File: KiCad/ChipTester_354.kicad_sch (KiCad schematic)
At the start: 3 parts, among them SW1 7101MD9AQE

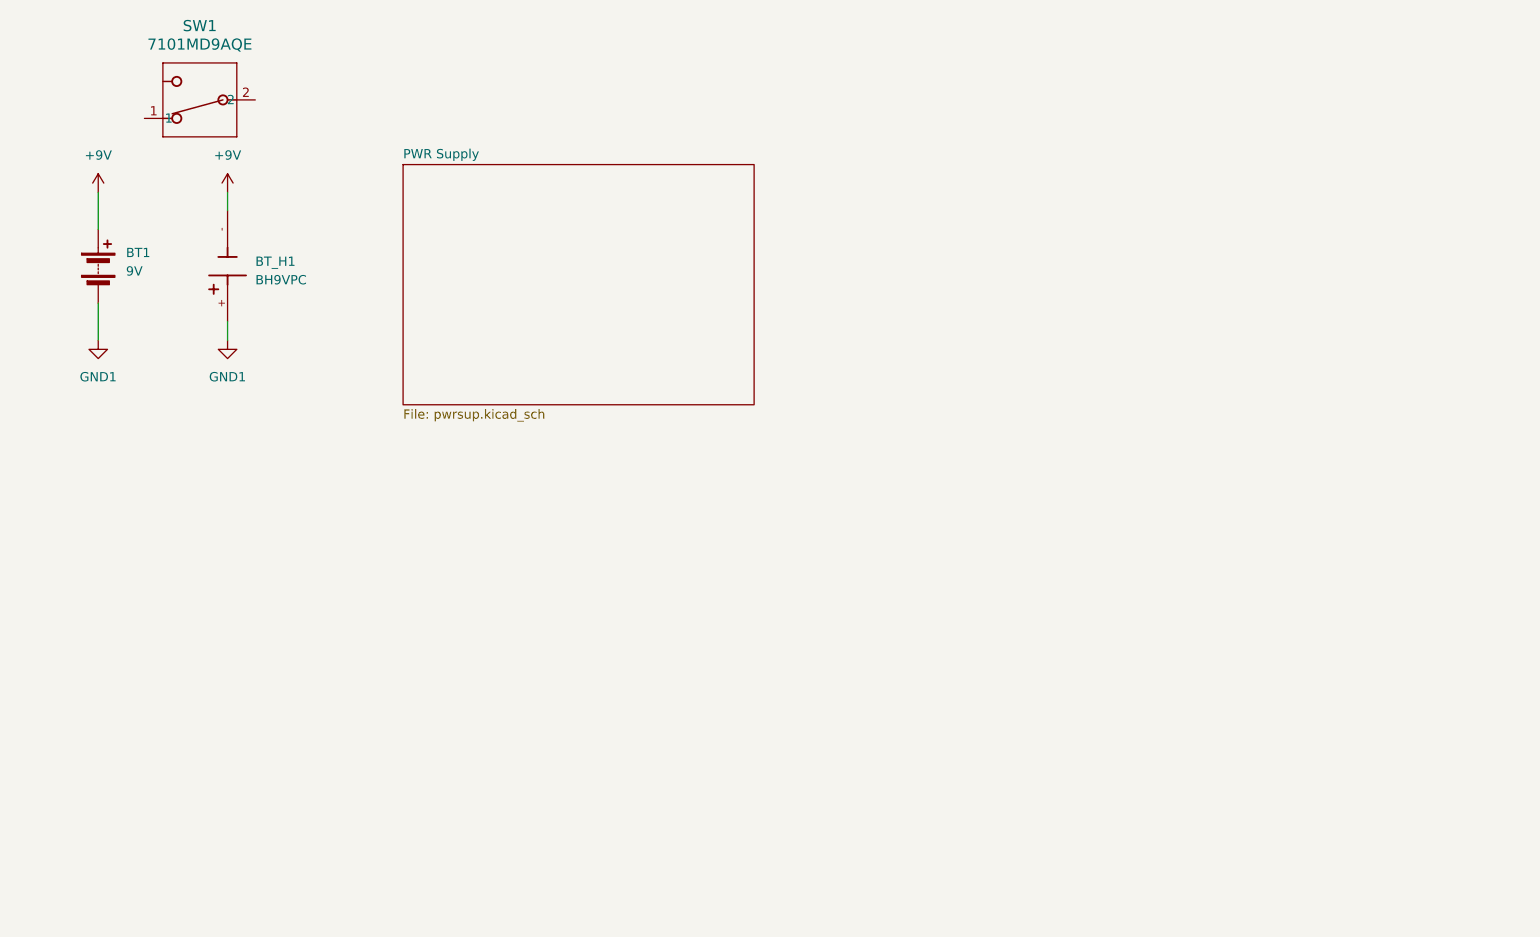
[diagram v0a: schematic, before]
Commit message: Finish power supply, make waveform generator.
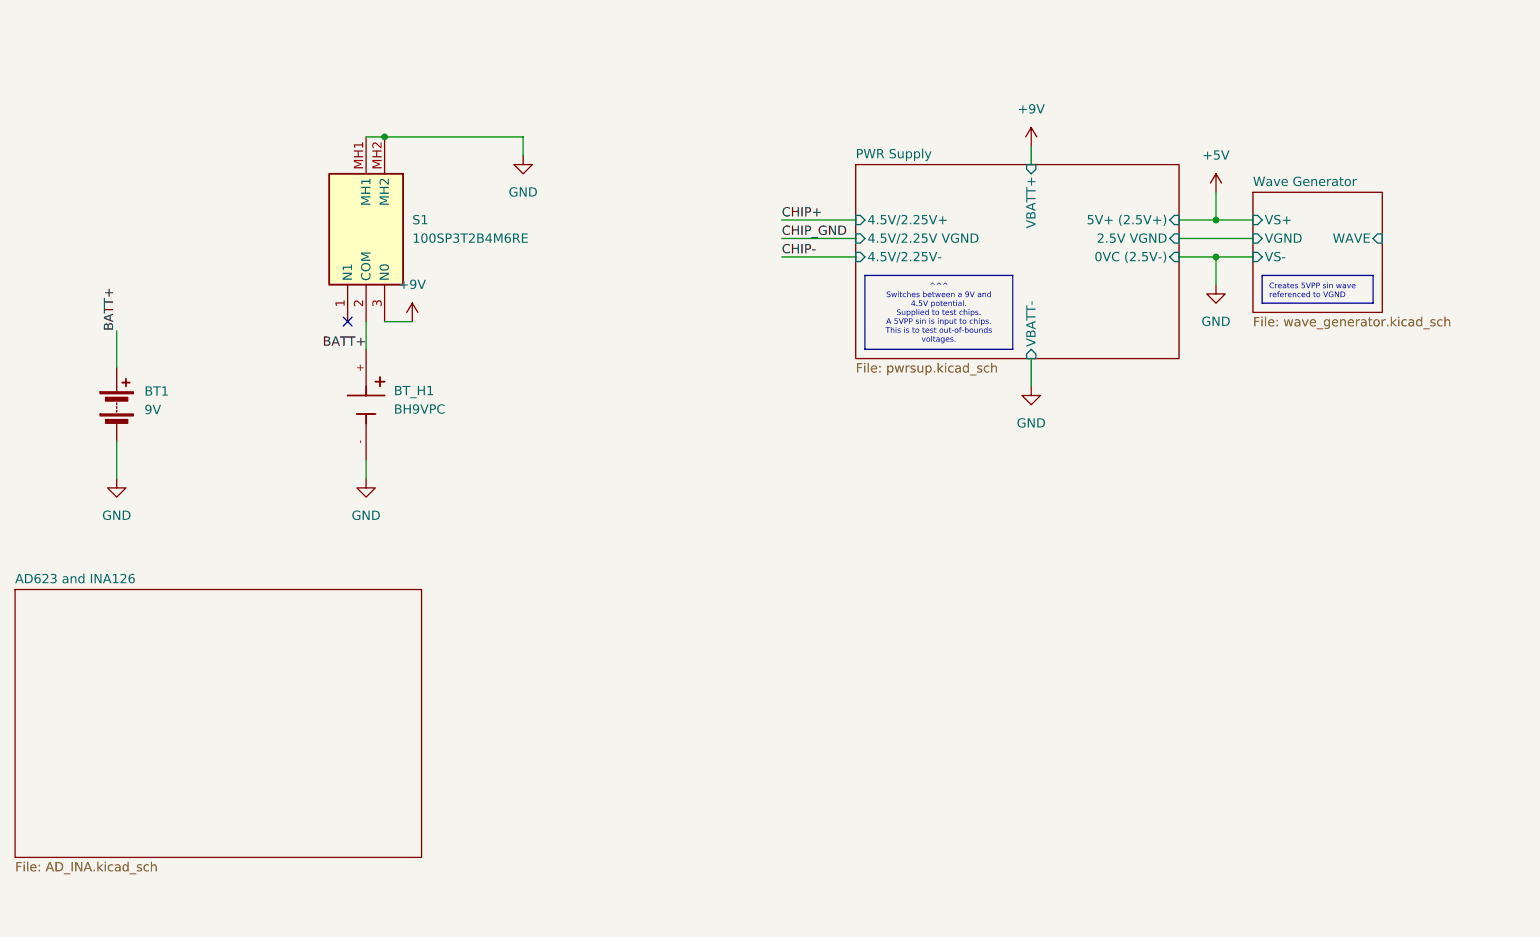
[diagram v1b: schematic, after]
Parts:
- removed SW1: 7101MD9AQE, SW3_7101MD9AQE_CNK, symbol 7101MD9AQE:7101MD9AQE
- added S1: 100SP3T2B4M6RE, 100SP3T2B4M6RE, symbol 100SP3T2B4M6RE:100SP3T2B4M6RE
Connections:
- net +9V: now also S1.3 (N0); no longer BT1.1 (+), BT_H1.-
- net GND1 renamed BATT+
- net BATT+: now also BT1.1 (+), S1.2 (COM); no longer BT1.2 (-)
- new net GND: BT1.2 (-), BT_H1.-, S1.MH1, S1.MH2
- no-connect marks 0 -> 1
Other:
- added sheet AD623 and INA126 (AD_INA.kicad_sch)
- added sheet Wave Generator (wave_generator.kicad_sch)
- sheet PWR Supply ports: added 0VC (2.5V-), 2.5V VGND, 4.5V/2.25V VGND, 4.5V/2.25V+, 4.5V/2.25V-, 5V+ (2.5V+), VBATT+, VBATT-; removed none
- moved on the sheet: BT1, BT_H1

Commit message: started edited pcb layout
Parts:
- S1: footprint 100SP3T2B4M6RE -> 100SP3T2B4M6RE:100SP3T2B4M6RE
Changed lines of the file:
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@@
 			)
 		)
-		(property "Footprint" "100SP3T2B4M6RE"
+		(property "Footprint" "100SP3T2B4M6RE:100SP3T2B4M6RE"
 			(at -14.91 48.26 0)
 			(effects

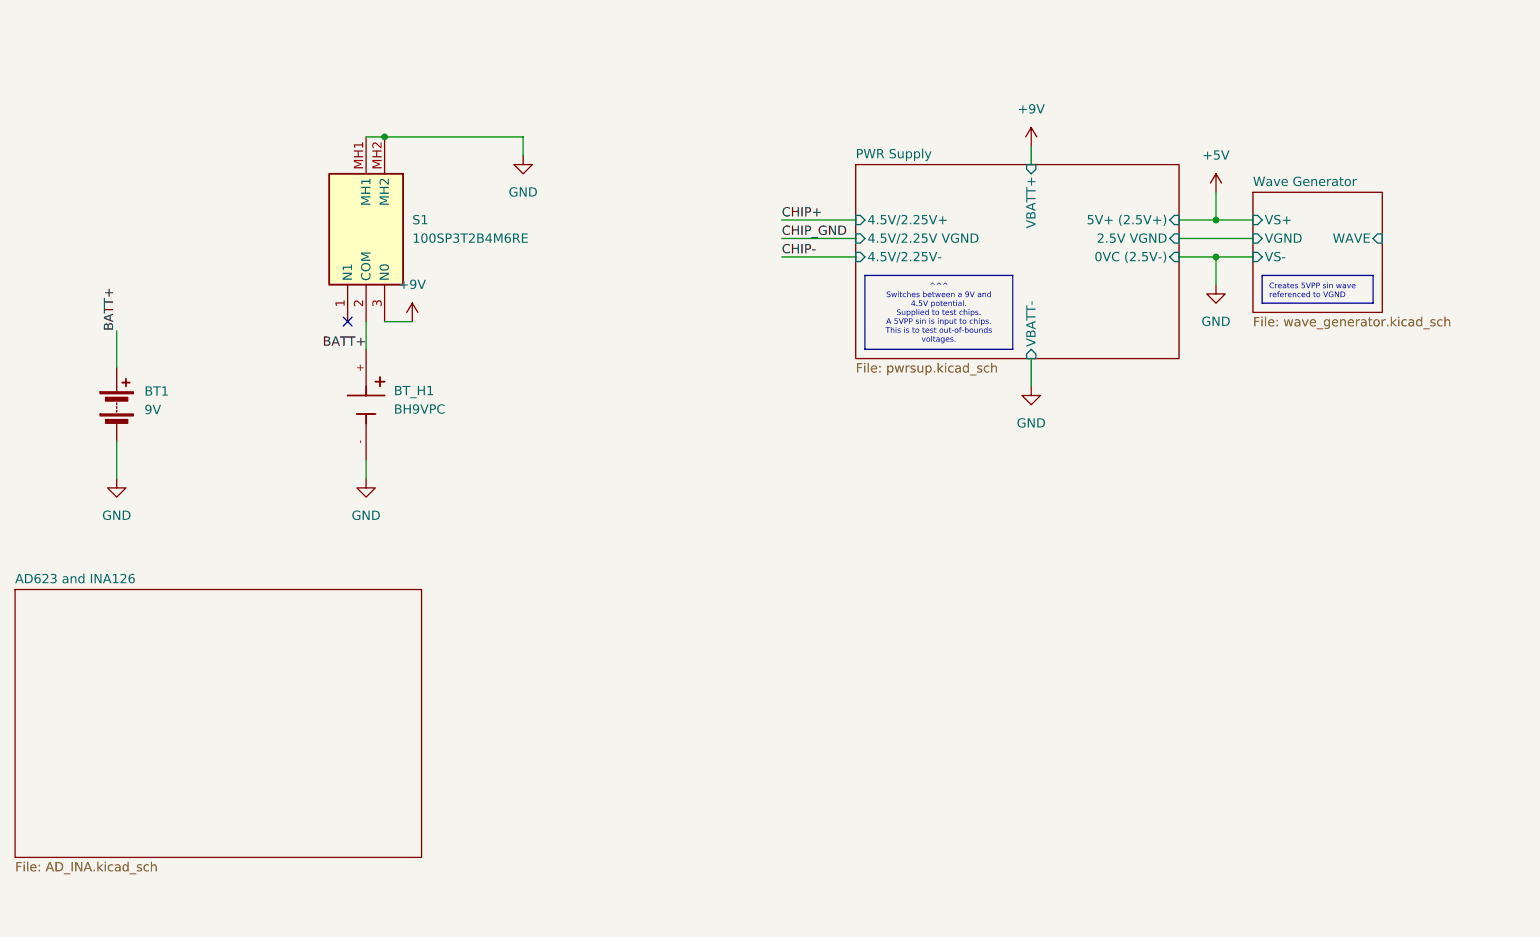
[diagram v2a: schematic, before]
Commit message: ADD AC623 and INA126 Test Circuitry
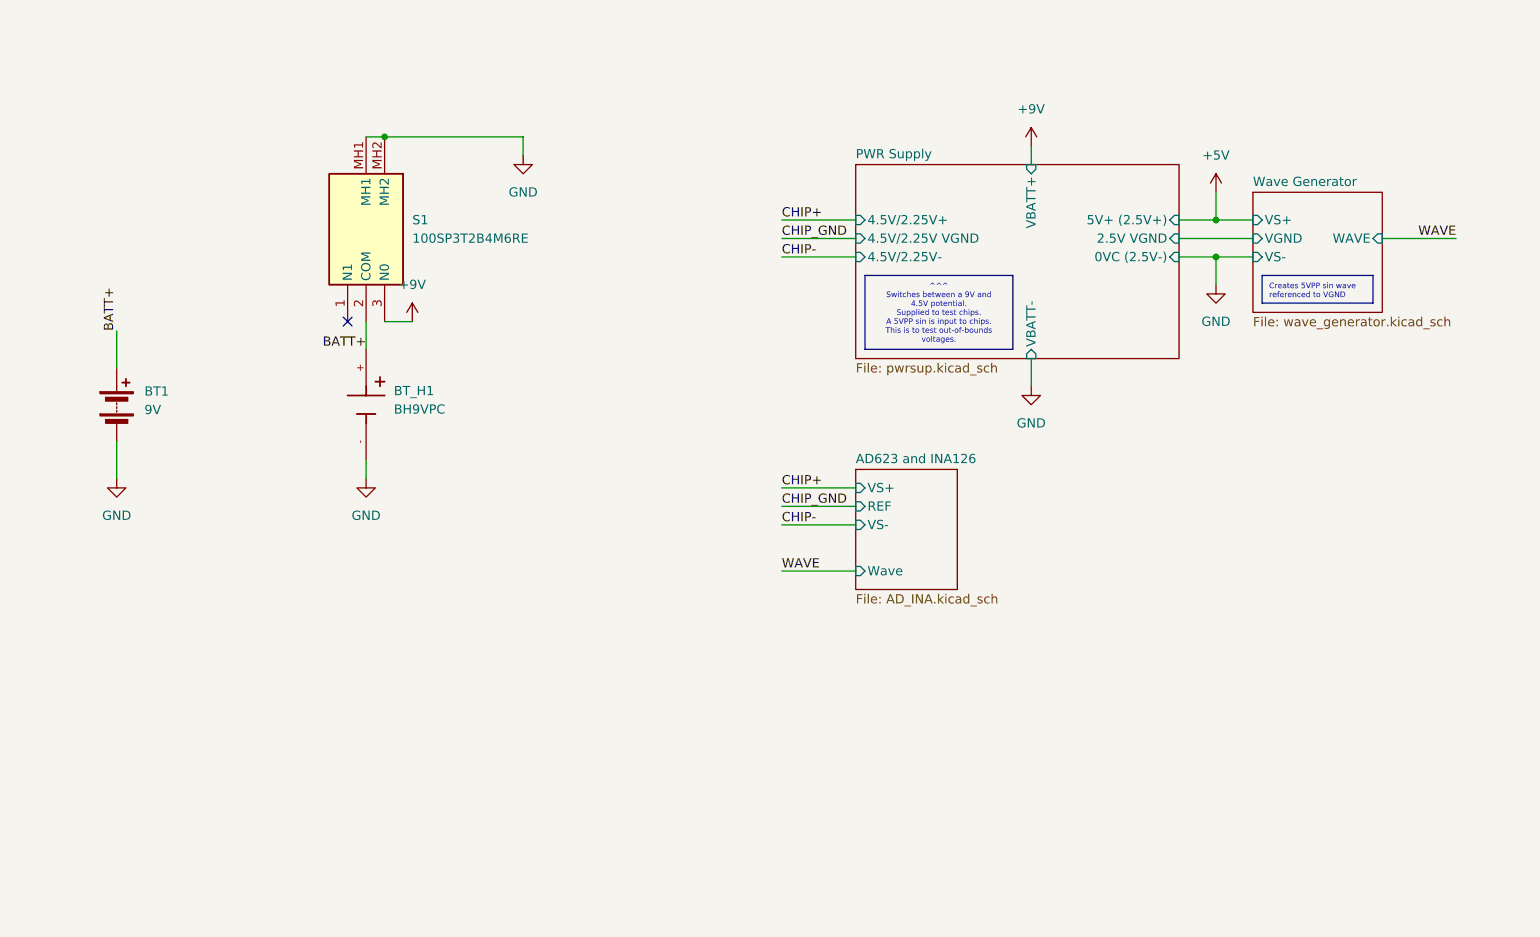
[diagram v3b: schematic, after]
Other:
- sheet AD623 and INA126 ports: added REF, VS+, VS-, Wave; removed none
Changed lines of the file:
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@@
+	(wire
+		(pts
+			(xy 217.17 40.64) (xy 227.33 40.64)
+		)
+		(stroke
+			(width 0)
+			(type default)
+		)
+	)
 	(wire
 		(pts
@@
 	(wire
 		(pts
+			(xy 144.78 86.36) (xy 134.62 86.36)
+		)
+		(stroke
+			(width 0)
+			(type default)
+		)
+	)
+	(wire
+		(pts
+			(xy 134.62 74.93) (xy 144.78 74.93)
+		)
+		(stroke
+			(width 0)
+			(type default)
+		)
+	)
+	(wire
+		(pts
 			(xy 189.23 43.18) (xy 194.31 43.18)
 		)
@@
 	(wire
 		(pts
+			(xy 134.62 80.01) (xy 144.78 80.01)
+		)
+		(stroke
+			(width 0)
+			(type default)
+		)
+	)
+	(wire
+		(pts
 			(xy 77.47 71.12) (xy 77.47 73.66)
 		)
@@
 			(width 0)
 			(type default)
+		)
+	)
+	(wire
+		(pts
+			(xy 134.62 77.47) (xy 144.78 77.47)
+		)
+		(stroke
+			(width 0)
+			(type default)
+		)
+	)
+	(label "CHIP_GND"
+		(at 134.62 77.47 0)
+		(effects
+			(font
+				(size 1.27 1.27)
+			)
+			(justify left bottom)
+		)
+	)
+	(label "WAVE"
+		(at 227.33 40.64 180)
+		(effects
+			(font
+				(size 1.27 1.27)
+			)
+			(justify right bottom)
+		)
+	)
+	(label "CHIP-"
+		(at 134.62 80.01 0)
+		(effects
+			(font
+				(size 1.27 1.27)
+			)
+			(justify left bottom)
 		)
 	)
@@
 	)
 	(label "CHIP+"
+		(at 134.62 74.93 0)
+		(effects
+			(font
+				(size 1.27 1.27)
+			)
+			(justify left bottom)
+		)
+	)
+	(label "CHIP+"
 		(at 134.62 38.1 0)
 		(effects
@@
 	(label "CHIP_GND"
 		(at 134.62 40.64 0)
+		(effects
+			(font
+				(size 1.27 1.27)
+			)
+			(justify left bottom)
+		)
+	)
+	(label "WAVE"
+		(at 134.62 86.36 0)
 		(effects
 			(font
@@
 	)
 	(sheet
-		(at 29.21 88.9)
-		(size 55.88 36.83)
+		(at 144.78 72.39)
+		(size 13.97 16.51)
 		(exclude_from_sim no)
 		(in_bom yes)
@@
 		)
 		(property "Sheetname" "AD623 and INA126"
-			(at 29.21 88.1884 0)
+			(at 144.78 71.6784 0)
 			(effects
 				(font
@@
 		)
 		(property "Sheetfile" "AD_INA.kicad_sch"
-			(at 29.21 126.3146 0)
+			(at 144.78 89.4846 0)
 			(effects
 				(font
@@
 			)
 		)
+		(pin "VS+" input
+			(at 144.78 74.93 180)
+			(effects
+				(font
+					(size 1.27 1.27)
+				)
+				(justify left)
+			)
+		)
+		(pin "VS-" input
+			(at 144.78 80.01 180)
+			(effects
+				(font
+					(size 1.27 1.27)
+				)
+				(justify left)
+			)
+		)
+		(pin "REF" input
+			(at 144.78 77.47 180)
+			(effects
+				(font
+					(size 1.27 1.27)
+				)
+				(justify left)
+			)
+		)
+		(pin "Wave" input
+			(at 144.78 86.36 180)
+			(effects
+				(font
+					(size 1.27 1.27)
+				)
+				(justify left)
+			)
+		)

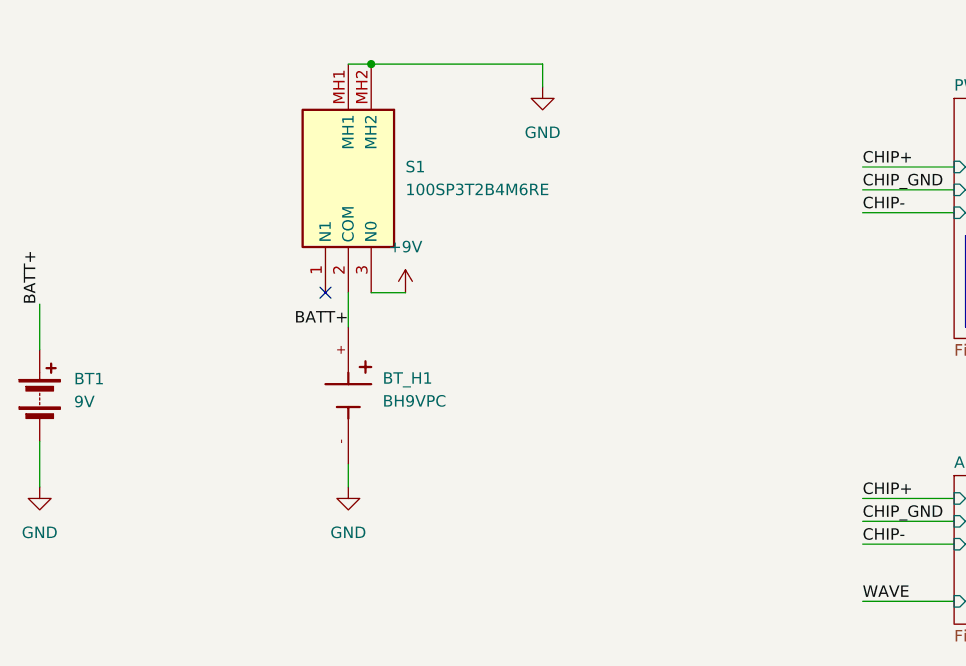
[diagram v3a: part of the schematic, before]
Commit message: Update battery switch to dpdt.
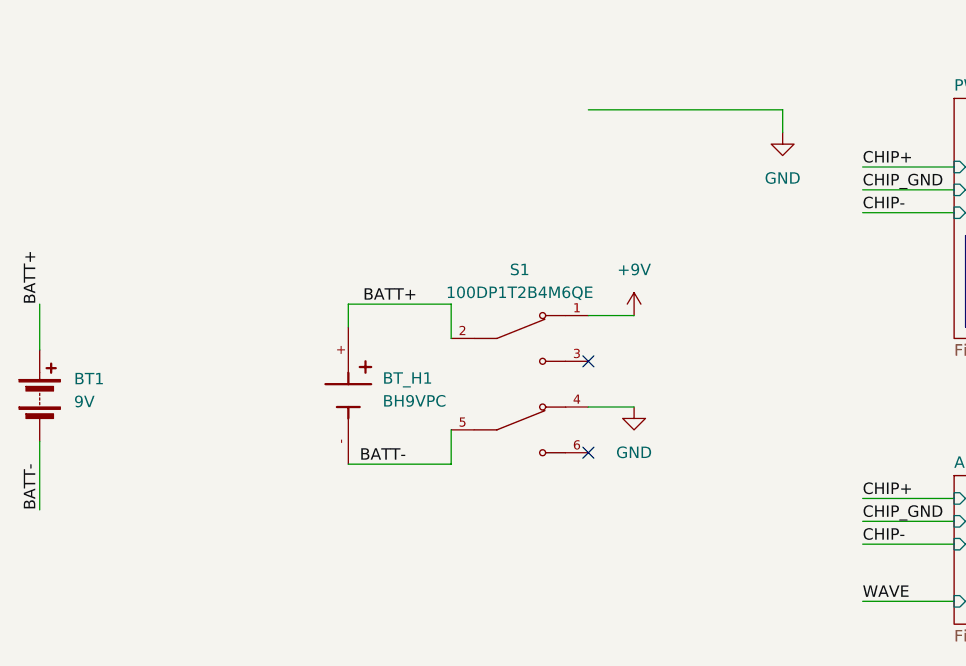
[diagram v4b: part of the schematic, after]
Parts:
- removed S1: 100SP3T2B4M6RE, 100SP3T2B4M6RE:100SP3T2B4M6RE, symbol 100SP3T2B4M6RE:100SP3T2B4M6RE
- added S1: 100DP1T2B4M6QE, 100DP1T2B4M6QE:SW_100DP1T2B4M6QE, symbol 100DP1T2B4M6QE:100DP1T2B4M6QE
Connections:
- net +9V: now also S1.1
- net BATT+: now also S1.2
- net GND: now also S1.4; no longer BT1.2 (-), BT_H1.-
- new net BATT-: BT1.2 (-), BT_H1.-, S1.5
- no-connect marks 1 -> 2
